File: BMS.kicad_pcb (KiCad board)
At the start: 2 copper layers, 11 x 14 mm, 122 parts, among them J1 Conn_01x10_Male, J2 Conn_01x10_Male, J3 Conn_01x03_Male, J4 Conn_01x05_Male, J5 Conn_01x01_Male, J6 Conn_01x03_Male, J7 Conn_01x01_Male, J8 Conn_01x01_Male, J9 Conn_01x01_Male, Q1 BSS308PE, Q10 BSS308PE, Q11 BSS308PE, Q12 BSS308PE, Q13 BSS308PE, Q14 BSS308PE, Q15 BSS308PE, Q16 BSS308PE, Q17 BSS308PE, Q18 BSS308PE, Q19 BCP56, Q2 BSS308PE, Q20 IPT012N08N5, Q21 IPT012N08N5, Q3 BSS308PE, Q4 BSS308PE, Q5 BSS308PE, Q6 BSS308PE, Q7 BSS308PE, Q8 BSS308PE, Q9 BSS308PE, U1 LTC6813-1, U2 ACS758xCB-150B-PSS, U3 ACS758xCB-150B-PSS

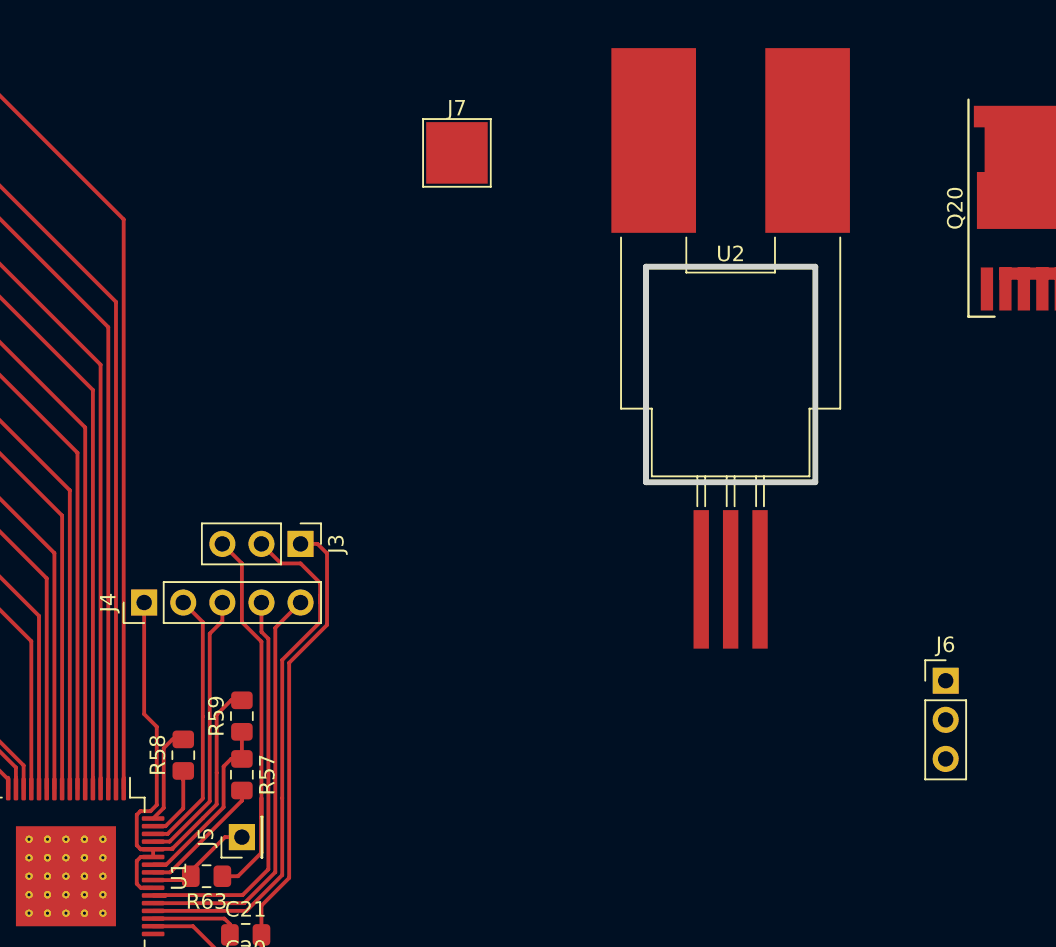
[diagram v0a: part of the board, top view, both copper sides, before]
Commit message: Remove diode on charge input
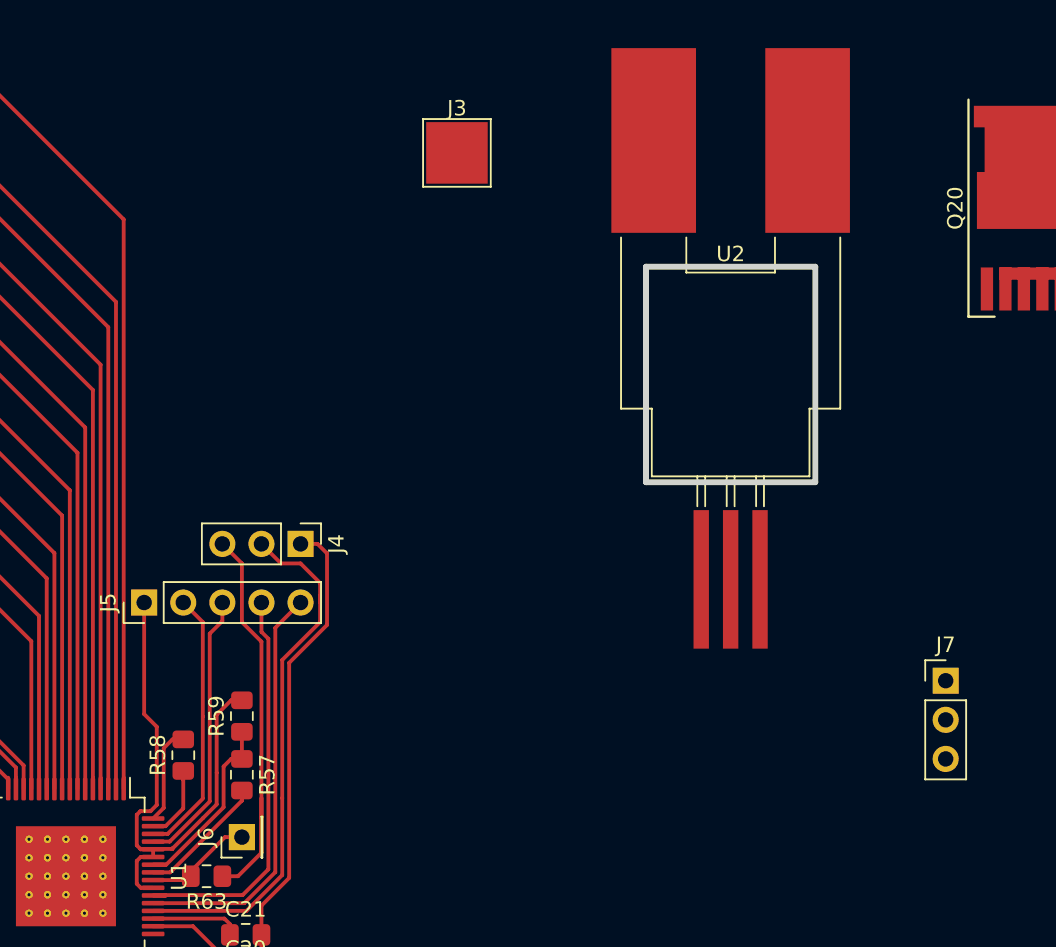
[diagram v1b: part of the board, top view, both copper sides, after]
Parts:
- C23: value 100nF -> 100n
- R57, R59: value R -> 1k
- renumbered J7 to J3, J3 to J4, J4 to J5, J5 to J6, J6 to J7
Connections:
- C1 pad 2: Net-(C1-Pad2) -> VPP
- J1 pad 2: VPP -> Net-(J1-Pad2)
- J8 pad 1: Net-(D1-Pad1) -> Net-(J8-Pad1)
- Q1 pad 2: VPP -> Net-(J1-Pad2)
- Q21 pad 2: Net-(D1-Pad2) -> Net-(J8-Pad1)
- R19 pad 1: Net-(C1-Pad2) -> VPP
- R19 pad 2: VPP -> Net-(J1-Pad2)
- R20 pad 2: VPP -> Net-(J1-Pad2)
- U1 pad 1: Net-(C1-Pad2) -> VPP
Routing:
- net Net-(C1-Pad2): track 54.6 -> 0.00 mm
- net VPP: track 5.21 -> 54.6 mm
- net Net-(J5-Pad5): track 27.0 -> 0.00 mm
- net Net-(J4-Pad5): track 0.00 -> 27.0 mm
- net Net-(J5-Pad4): track 26.5 -> 0.00 mm
- net Net-(J4-Pad4): track 0.00 -> 26.5 mm
- net Net-(J5-Pad3): track 18.0 -> 0.00 mm
- net Net-(J4-Pad3): track 0.00 -> 18.0 mm
- net Net-(J5-Pad2): track 17.4 -> 0.00 mm
- net Net-(J4-Pad2): track 34.7 -> 52.1 mm
- net Net-(J1-Pad2): track 0.00 -> 5.21 mm

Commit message: backup
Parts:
- removed D1: C5D50065D, Package_TO_SOT_THT:TO-247-3_Vertical
- R63: footprint Resistor_SMD:R_0805_2012Metric_Pad1.15x1.40mm_HandSolder -> Resistor_SMD:R_1206_3216Metric_Pad1.42x1.75mm_HandSolder
- moved J9 123.0 mm to (182.9, 121.9), turned to 270 degrees
- moved U3 120.5 mm to (151.6, 113.0), turned to 270 degrees
- moved R61 119.3 mm to (148.6, 76.0), turned to 90 degrees
- moved R60 115.0 mm to (148.6, 71.1), turned to 90 degrees
- moved J8 90.3 mm to (156.2, 99.1), turned to 270 degrees
- moved Q21 62.3 mm to (161.4, 86.9), turned to 0 degrees
- moved R65 57.2 mm to (148.6, 81.0), turned to 270 degrees
- moved R64 55.3 mm to (148.6, 85.3), turned to 270 degrees
- moved Q20 38.8 mm to (164.4, 69.7)
- moved J7 38.2 mm to (144.8, 73.7)
- moved J4 26.7 mm to (142.2, 88.9), turned to 180 degrees
- moved U2 17.4 mm to (151.6, 50.9), turned to 270 degrees
- moved J3 14.9 mm to (165.1, 31.8), turned to 270 degrees
- moved Q19 7.09 mm to (146.1, 95.2)
- moved R63 6.33 mm to (139.9, 80.0)
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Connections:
- C1 pad 2: VPP -> Net-(C1-Pad2)
- J1 pad 2: Net-(J1-Pad2) -> VPP
- J3 pad 1: Net-(J3-Pad1) -> GND
- Q1 pad 2: Net-(J1-Pad2) -> VPP
- R19 pad 1: VPP -> Net-(C1-Pad2)
- R19 pad 2: Net-(J1-Pad2) -> VPP
- R20 pad 2: Net-(J1-Pad2) -> VPP
- U1 pad 1: VPP -> Net-(C1-Pad2)
- U1 pad 53: Net-(J5-Pad4) -> Net-(J5-Pad5)
- U1 pad 54: Net-(J5-Pad5) -> Net-(J5-Pad4)
- U1 pad 61: Net-(J5-Pad2) -> Net-(J5-Pad3)
- U1 pad 62: Net-(J5-Pad3) -> Net-(J5-Pad2)
- U2 pad 3: Net-(U1-Pad39) -> Net-(U1-Pad40)
- U2 pad 5: Net-(J3-Pad1) -> GND
- U3 pad 3: Net-(U1-Pad40) -> Net-(U1-Pad39)
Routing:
- net GND: track 279.5 -> 424.1 mm
- net VCC: track 27.8 -> 112.0 mm
- net Net-(C1-Pad2): track 0.00 -> 59.2 mm
- net Net-(U1-Pad40): track 0.00 -> 46.0 mm
- net Net-(J4-Pad2): track 52.1 -> 11.0 mm
- net Net-(Q20-Pad2): track 0.00 -> 38.3 mm
- net Net-(U1-Pad39): track 0.00 -> 33.2 mm
- net Net-(J5-Pad5): track 0.00 -> 28.7 mm
- net Net-(J4-Pad5): track 27.0 -> 0.00 mm
- net Net-(J4-Pad4): track 26.5 -> 0.00 mm
- net Net-(J5-Pad4): track 0.00 -> 25.6 mm
- net VPP: track 54.6 -> 34.3 mm
- net Net-(J2-Pad10): track 15.2 -> 35.0 mm
- net Net-(J5-Pad3): track 0.00 -> 18.5 mm
- net Net-(J4-Pad3): track 18.0 -> 0.00 mm
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- added copper zone on F.Cu, net GND
- added copper zone on F.Cu, net Net-(J8-Pad1)
- added copper zone on F.Cu, net Net-(Q20-Pad2)
- added copper zone on F.Cu, net Net-(Q20-Pad3)
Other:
- board size 11 x 14 mm -> 14 x 11 mm

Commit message: First routing
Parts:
- added J4: Conn_01x08_Male, Connector_PinHeader_2.54mm:PinHeader_1x08_P2.54mm_Vertical, F.Cu at (129.5, 95.2)
- moved C23 12.6 mm to (148.3, 88.9), turned to 180 degrees
- moved R62 6.67 mm to (145.0, 100.3), turned to 0 degrees
- moved J10 5.24 mm to (177.8, 123.2)
- moved C22 4.45 mm to (139.7, 96.5), turned to 90 degrees
- renumbered J9 to J10, J4 to J5, J5 to J6, J6 to J7, J7 to J9
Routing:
- net VPP: track 34.3 -> 186.0 mm
- net GND: track 424.1 -> 518.4 mm
- net Net-(J4-Pad8): track 0.00 -> 25.5 mm
- net Net-(J4-Pad7): track 0.00 -> 23.7 mm
- net Net-(J4-Pad6): track 0.00 -> 20.1 mm
- net Net-(J4-Pad5): track 0.00 -> 17.2 mm
- net Net-(J4-Pad4): track 0.00 -> 14.5 mm
- net Net-(J4-Pad3): track 0.00 -> 11.8 mm
- net Net-(J4-Pad2): track 0.00 -> 9.79 mm
- net VCC: track 112.0 -> 117.6 mm
- net Net-(C23-Pad1): track 16.7 -> 19.8 mm
- net Net-(U1-Pad39): track 33.2 -> 34.6 mm
- net Net-(C17-Pad2): track 26.8 -> 28.0 mm
- added copper zone on F.Cu, net Net-(J10-Pad1)

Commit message: First Version (Ordered)
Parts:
- added Q19: IPT012N08N5, Package_TO_SOT_SMD:Infineon_PG-HSOF-8-1, F.Cu at (164.4, 54.6)
- added R60: 4k7, Resistor_SMD:R_0805_2012Metric_Pad1.15x1.40mm_HandSolder, F.Cu at (148.6, 66.3)
- added R61: 200, Resistor_SMD:R_0805_2012Metric_Pad1.15x1.40mm_HandSolder, F.Cu at (148.6, 62.5)
- J9: value Conn_01x03_Male -> Conn_01x04_Male; footprint Connector_PinHeader_2.54mm:PinHeader_1x03_P2.54mm_Vertical -> Connector_PinHeader_2.54mm:PinHeader_1x04_P2.54mm_Vertical
- moved U2 14.0 mm to (151.6, 36.9)
- moved J3 11.4 mm to (176.5, 31.8)
- moved J9 2.54 mm to (144.8, 71.1)
- renumbered Q19 to Q20, Q20 to Q21, Q21 to Q22, R60 to R62, R61 to R63, R62 to R64, R63 to R65, R64 to R66, R65 to R67
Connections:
- J2 pad 10: Net-(J2-Pad10) -> GND
- Q21 pad 3: Net-(Q20-Pad3) -> Net-(Q19-Pad3)
- R18 pad 2: Net-(J2-Pad10) -> GND
- R38 pad 1: GND -> Net-(R38-Pad1)
- R38 pad 2: Net-(J2-Pad10) -> GND
- R63 pad 1: Net-(J9-Pad2) -> Net-(J9-Pad3)
- R67 pad 1: Net-(J9-Pad3) -> Net-(J9-Pad4)
- U1 pad 38: GND -> Net-(R38-Pad1)
- U2 pad 4: Net-(Q20-Pad3) -> Net-(Q19-Pad2)
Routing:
- net GND: track 518.4 -> 589.9 mm
- net Net-(R38-Pad1): track 0.00 -> 41.0 mm
- net Net-(Q19-Pad1): track 0.00 -> 36.3 mm
- net Net-(J2-Pad10): track 35.0 -> 0.00 mm
- net Net-(Q19-Pad2): track 0.00 -> 14.7 mm
- net Net-(U1-Pad40): track 46.0 -> 60.3 mm
- net Net-(Q19-Pad3): track 0.00 -> 14.1 mm
- net VCC: track 117.6 -> 131.2 mm
- net Net-(J9-Pad2): track 4.13 -> 14.3 mm
- net Net-(Q20-Pad3): track 6.74 -> 0.00 mm
- net Net-(J8-Pad1): track 9.18 -> 13.9 mm
- net Net-(J9-Pad4): track 0.00 -> 4.67 mm
- net Net-(J9-Pad3): track 4.67 -> 4.13 mm
- added copper zone on F.Cu, net Net-(Q19-Pad2)
- added copper zone on F.Cu, net Net-(Q19-Pad3)
- removed copper zone on F.Cu, net Net-(J8-Pad1)
- removed copper zone on F.Cu, net Net-(Q20-Pad3)
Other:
- board size 14 x 11 mm -> 100.3 x 102.9 mm
- board text added: ":-)"
- board text added: "Prototyp"
